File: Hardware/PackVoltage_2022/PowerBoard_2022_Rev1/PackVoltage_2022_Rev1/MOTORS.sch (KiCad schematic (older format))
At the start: 63 parts

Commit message: added andersons
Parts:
- removed C? (x7): .1uF, symbol Device:C
- removed C? (x7): 10uF, symbol Device:C
- removed D? (x7): LED, symbol Device:LED
- removed F? (x7): 20, symbol Device:Fuse
- removed Q? (x7): BUK7M8R0-40EX, Package_TO_SOT_SMD:LFPAK33, symbol Transistor_FET:BUK7M8R0-40EX
- removed R? (x7): 5.1k, symbol Device:R
- removed R? (x7): 3300, symbol Device:R
- removed U? (x7): LT1910, symbol MRDT_ICs:LT1910
- removed U? (x7): INA281, Package_TO_SOT_SMD:SOT-23-5, symbol MRDT_ICs:INA281
- added C? (x7): .1uF, symbol Device:C
- added C? (x7): 10uF, symbol Device:C
- added D? (x7): LED, symbol Device:LED
- added F? (x7): 20, symbol Device:Fuse
- added Q? (x7): BUK7M8R0-40EX, Package_TO_SOT_SMD:LFPAK33, symbol Transistor_FET:BUK7M8R0-40EX
- added R? (x7): 5.1k, symbol Device:R
- added R? (x7): 3300, symbol Device:R
- added R? (x7): .0025, symbol Device:R
- added U? (x7): LT1910, symbol MRDT_ICs:LT1910
- added U? (x7): INA281, Package_TO_SOT_SMD:SOT-23-5, symbol MRDT_ICs:INA281
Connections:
- net 5V: now also R?.2, R?.2, R?.2, R?.2, R?.2, R?.2, R?.2, U?.5 (V+), U?.5 (V+), U?.5 (V+), U?.5 (V+), U?.5 (V+), U?.5 (V+), U?.5 (V+)
- net Anderson_M1: now also R?.2, U?.4 (-)
- net Anderson_M2: now also R?.2, U?.4 (-)
- net Anderson_M3: now also R?.2, U?.4 (-)
- net Anderson_M4: now also R?.2, U?.4 (-)
- net Anderson_M5: now also R?.2, U?.4 (-)
- net Anderson_M6: now also R?.2, U?.4 (-)
- net Anderson_Spare: now also R?.2, U?.4 (-)
- net Driver_M1: now also U?.4 (IN)
- net Driver_M2: now also U?.4 (IN)
- net Driver_M3: now also U?.4 (IN)
- net Driver_M4: now also U?.4 (IN)
- net Driver_M5: now also U?.4 (IN)
- net Driver_M6: now also U?.4 (IN)
- net Driver_Spare: now also U?.4 (IN)
- net GND: now also C?.2, C?.2, C?.2, C?.2, C?.2, C?.2, C?.2, C?.2, C?.2, C?.2, C?.2, C?.2, C?.2, C?.2, D?.1 (K), D?.1 (K), D?.1 (K), D?.1 (K), D?.1 (K), D?.1 (K), D?.1 (K), U?.1 (GND), U?.1 (GND), U?.1 (GND), U?.1 (GND), U?.1 (GND), U?.1 (GND), U?.1 (GND), U?.2 (GND), U?.2 (GND), U?.2 (GND), U?.2 (GND), U?.2 (GND), U?.2 (GND), U?.2 (GND)
- net PV: now also F?.1, F?.1, F?.1, F?.1, F?.1, F?.1, F?.1
- new net: R?.1, U?.3 (FAULT) (x7)
- new net: C?.1, U?.2 (TIMER) (x7)
- new net: Q?.4 (G), U?.5 (GATE) (x7)
- new net: C?.1, F?.2, Q?.5 (D), U?.6 (SENSE), U?.8 (V+) (x7)
- new net: Q?.1 (S), Q?.2 (S), Q?.3 (S), R?.1, R?.2, U?.3 (+) (x7)
- new net: D?.2 (A), R?.1 (x7)
- new net Current_Sensor_M1: U?.1
- new net Current_Sensor_M2: U?.1
- new net Current_Sensor_M3: U?.1
- new net Current_Sensor_M4: U?.1
- new net Current_Sensor_M5: U?.1
- new net Current_Sensor_M6: U?.1
- new net Current_Sensor_Spare: U?.1

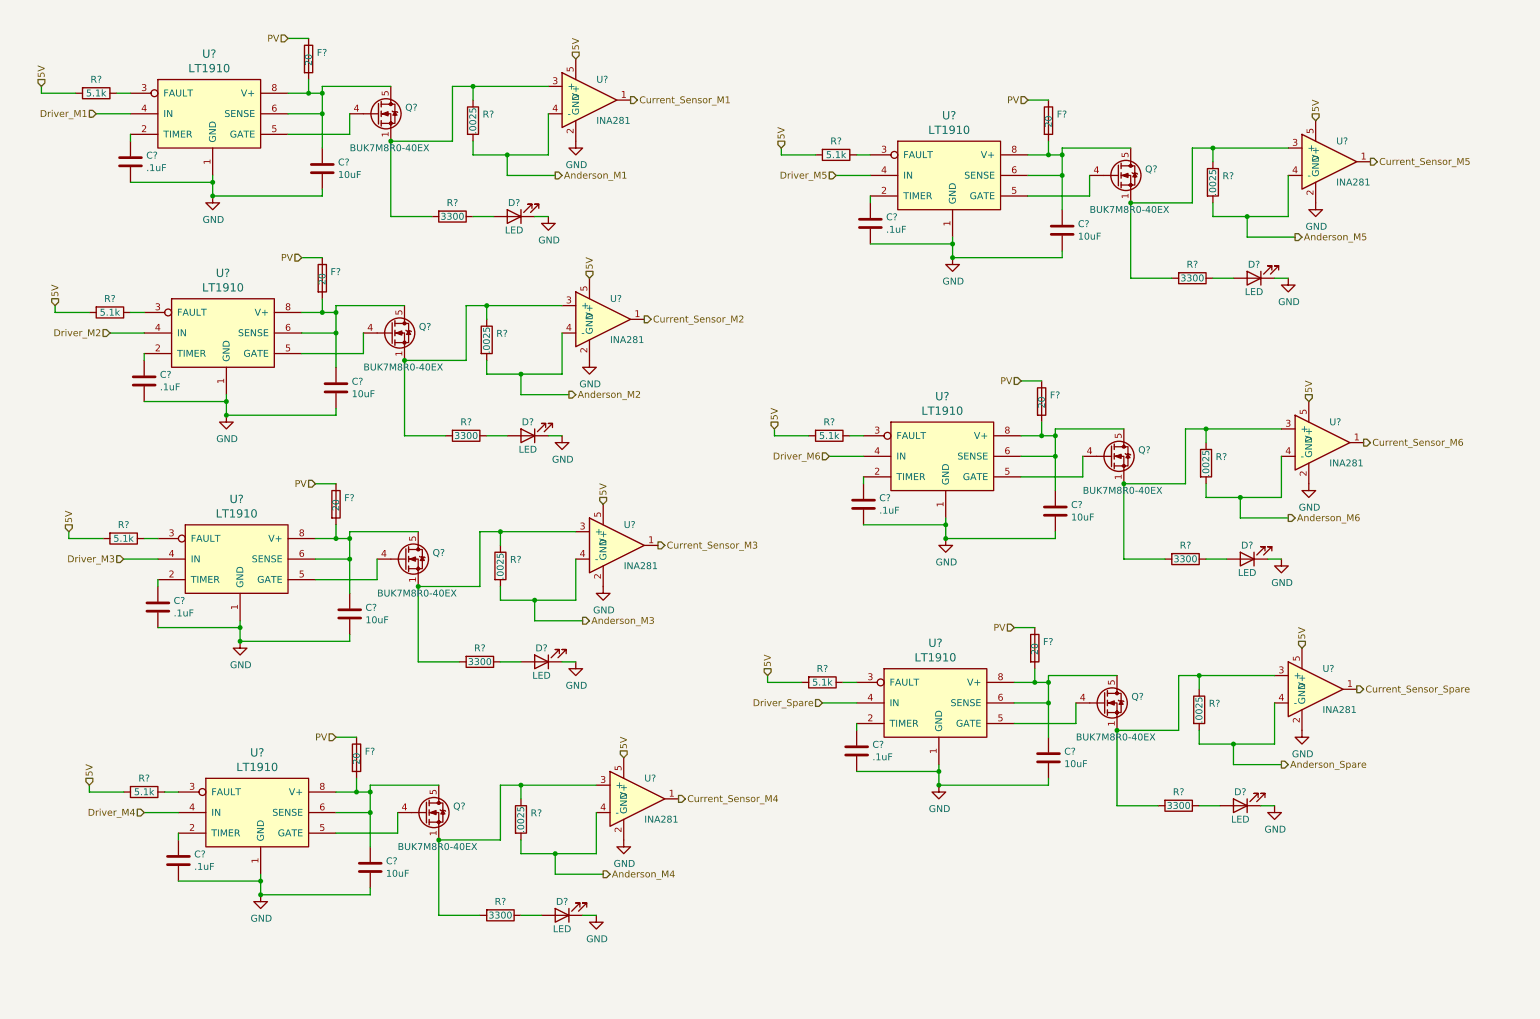
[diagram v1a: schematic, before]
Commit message: added 12V anderson
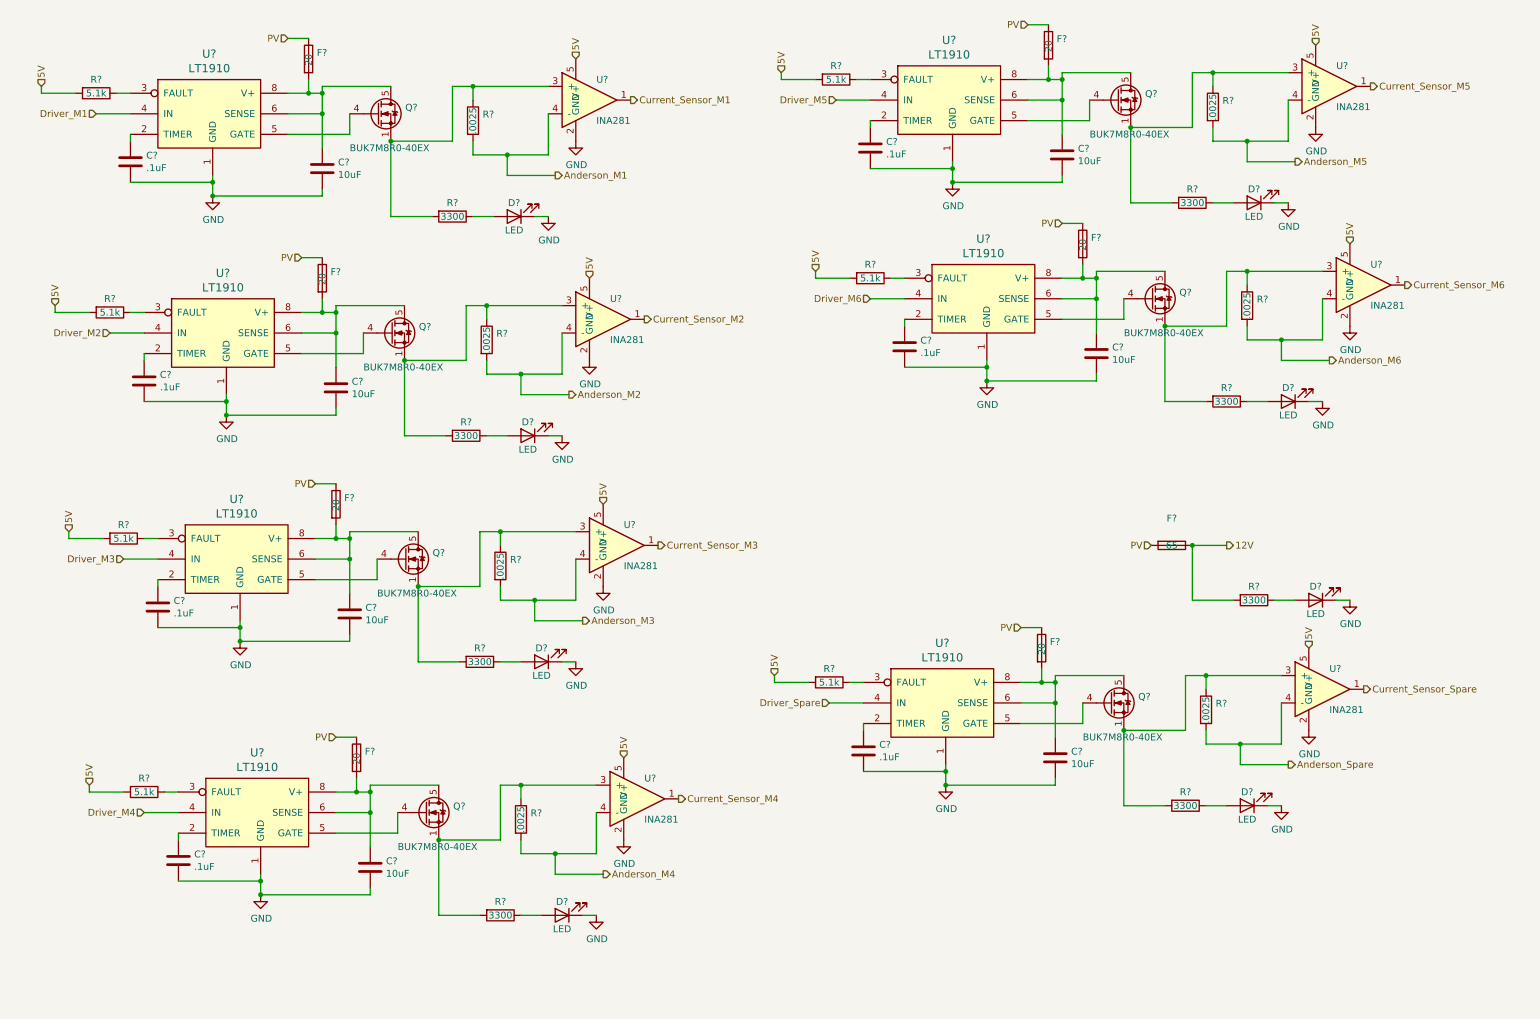
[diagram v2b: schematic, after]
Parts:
- added D?: LED, symbol Device:LED
- added F?: 65, symbol Device:Fuse
- added R?: 3300, symbol Device:R
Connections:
- net GND: now also D?.1 (K)
- net PV: now also F?.2
- new net: D?.2 (A), R?.1
- new net 12V: F?.1, R?.2
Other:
- moved on the sheet: C?, D?, F?, Q?, R?, U?

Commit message: Added POE
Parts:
- added C?: .1uF, symbol Device:C
- added C?: 10uF, symbol Device:C
- added D?: LED, symbol Device:LED
- added F?: 20, symbol Device:Fuse
- added Q?: BUK7M8R0-40EX, Package_TO_SOT_SMD:LFPAK33, symbol Transistor_FET:BUK7M8R0-40EX
- added R?: 5.1k, symbol Device:R
- added R?: 3300, symbol Device:R
- added R?: .0025, symbol Device:R
- added U?: LT1910, symbol MRDT_ICs:LT1910
- added U?: INA281, Package_TO_SOT_SMD:SOT-23-5, symbol MRDT_ICs:INA281
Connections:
- net 5V: now also R?.2, U?.5 (V+)
- net GND: now also C?.2, C?.2, D?.1 (K), U?.1 (GND), U?.2 (GND)
- net PV: now also F?.1
- new net: R?.1, U?.3 (FAULT)
- new net: C?.1, U?.2 (TIMER)
- new net: Q?.4 (G), U?.5 (GATE)
- new net: C?.1, F?.2, Q?.5 (D), U?.6 (SENSE), U?.8 (V+)
- new net: Q?.1 (S), Q?.2 (S), Q?.3 (S), R?.1, R?.2, U?.3 (+)
- new net: D?.2 (A), R?.1
- new net Anderson_POE: R?.2, U?.4 (-)
- new net Current_Sensor_POE: U?.1
- new net Driver_POE: U?.4 (IN)
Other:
- moved on the sheet: D?, F?, R?
